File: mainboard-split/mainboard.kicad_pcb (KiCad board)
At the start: 2 copper layers, 171.7 x 109 mm, 24 parts, among them J1 3V3 IN, J2 Conn_01x04, J3 Conn_01x03, J4 Conn_01x02, J5 3V3 OUT, J6 STICK POWER, SW1 SW_SPDT_MSM, SW2 SW_SPDT_MSM, SW3 SW_Push, SW4 SW_Push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

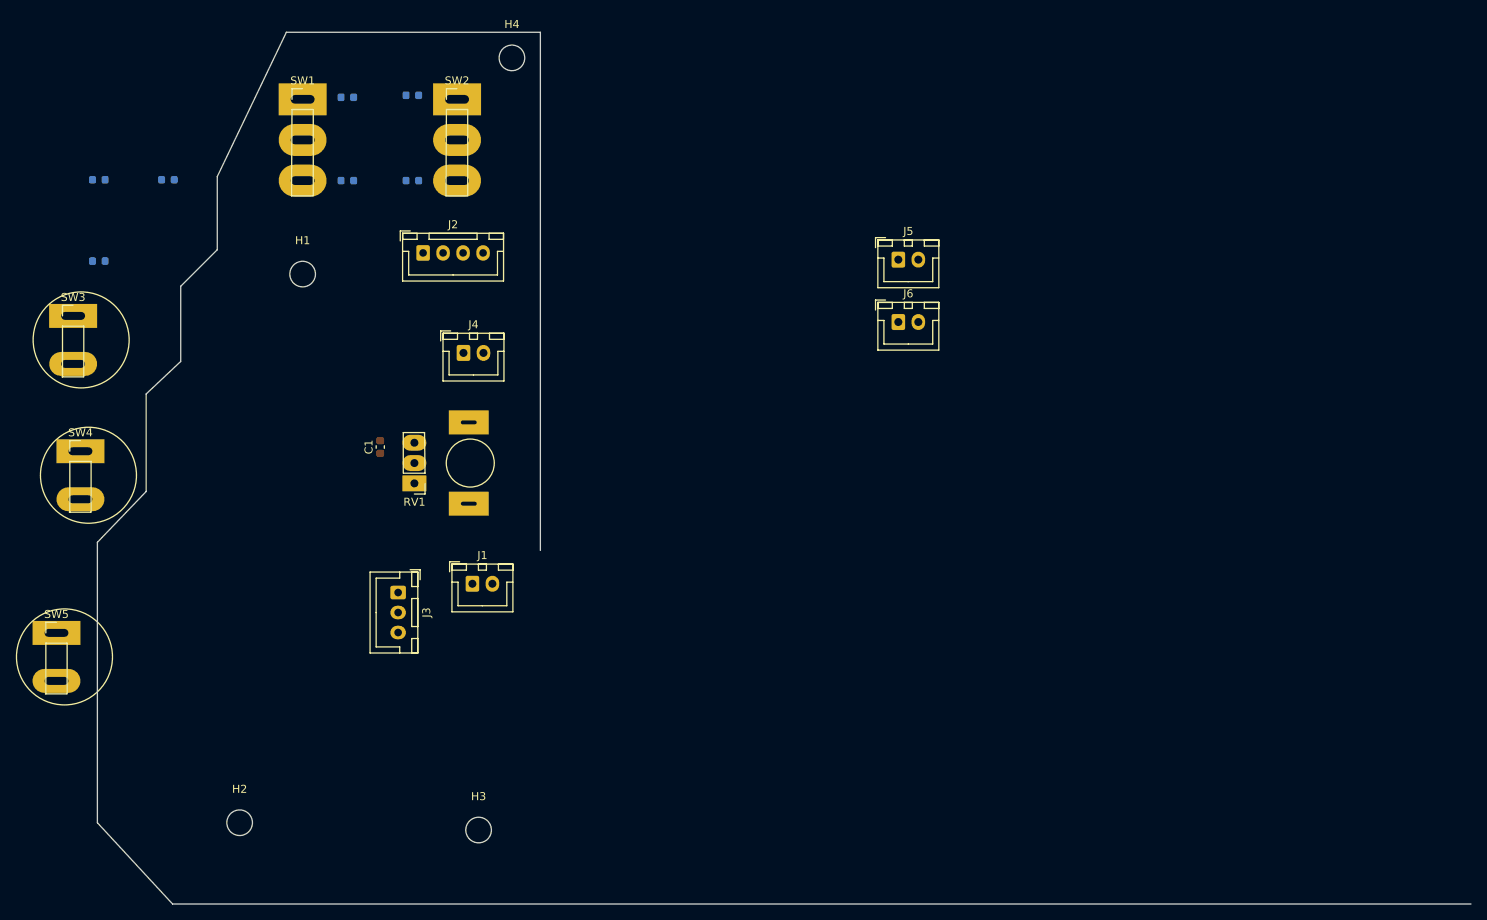
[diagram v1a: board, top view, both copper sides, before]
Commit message: Place switches on millimeter grid.
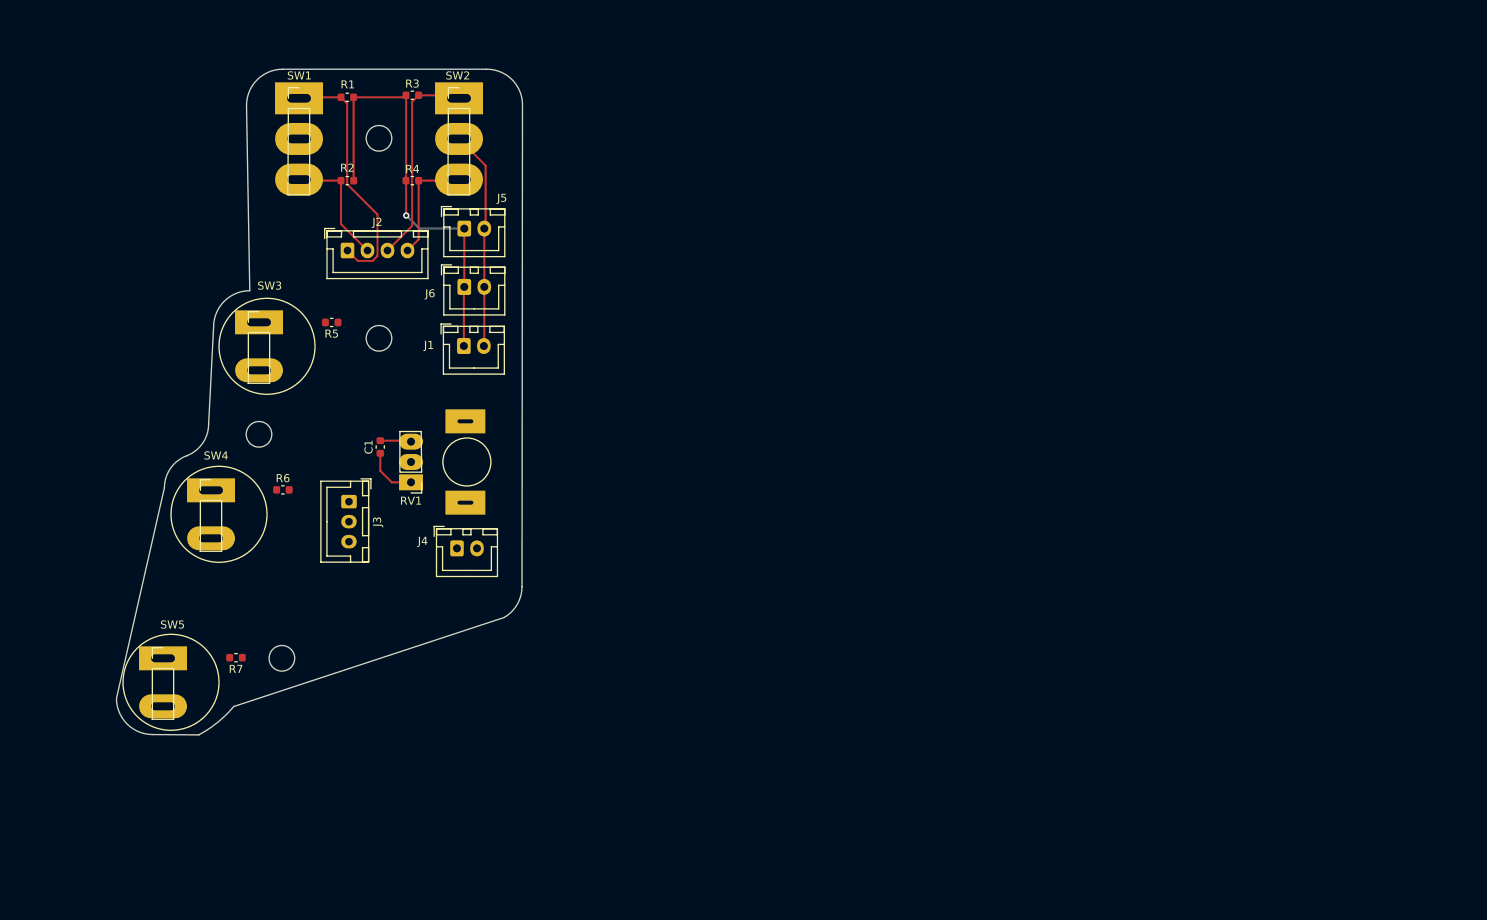
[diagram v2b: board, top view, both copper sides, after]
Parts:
- R1, R2, R3, R4, R5, R6, R7: moved to F.Cu
- moved R7 60.3 mm to (52.1, 204.9), turned to 180 degrees
- moved H3 56.6 mm to (55.0, 177.0)
- moved J6 54.4 mm to (80.7, 158.6)
- moved J5 54.4 mm to (80.7, 151.3)
- moved R6 36.7 mm to (58.0, 183.9), turned to 0 degrees
- moved R5 34.1 mm to (64.1, 163.0)
- moved J1 29.7 mm to (80.6, 166.0)
- moved J4 24.4 mm to (79.7, 191.3)
- moved SW3 23.2 mm to (55.0, 163.0)
- moved H2 21.2 mm to (57.9, 205.0)
- moved H4 19.4 mm to (70.0, 140.0)
- moved SW4 17.0 mm to (49.0, 184.0)
- moved SW5 13.7 mm to (43.0, 205.0)
- moved J3 12.9 mm to (66.2, 185.4)
- moved H1 12.5 mm to (70.0, 165.0)
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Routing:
- net +3V3: track 0.00 -> 61.4 mm, vias 0 -> 1
- net Net-(J2-Pin_1): track 0.00 -> 31.6 mm
- net GND: track 0.00 -> 31.2 mm
- net Net-(J2-Pin_3): track 0.00 -> 26.2 mm
- net Net-(J2-Pin_2): track 0.00 -> 15.4 mm
- net Net-(J2-Pin_4): track 0.00 -> 14.4 mm
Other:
- board size 171.7 x 109 mm -> 50.8 x 83.2 mm

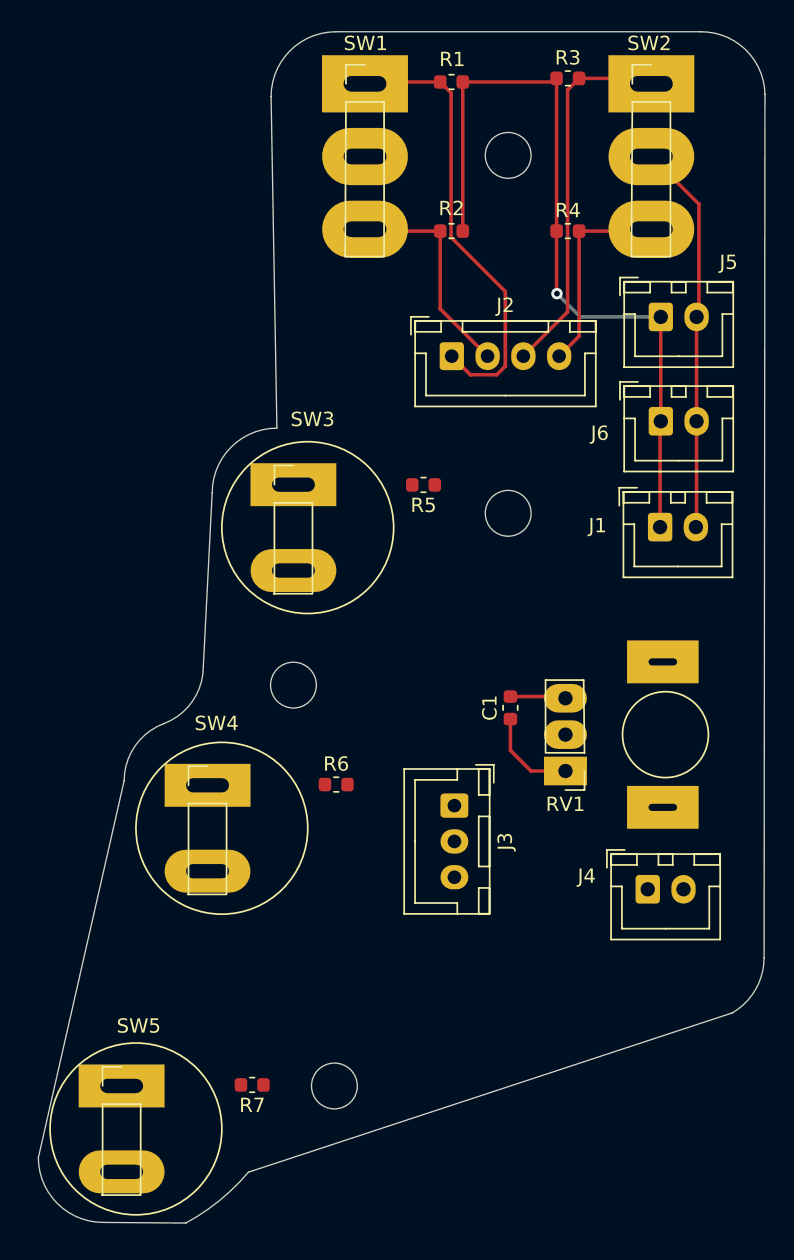
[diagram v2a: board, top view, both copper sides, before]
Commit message: Improve outline.
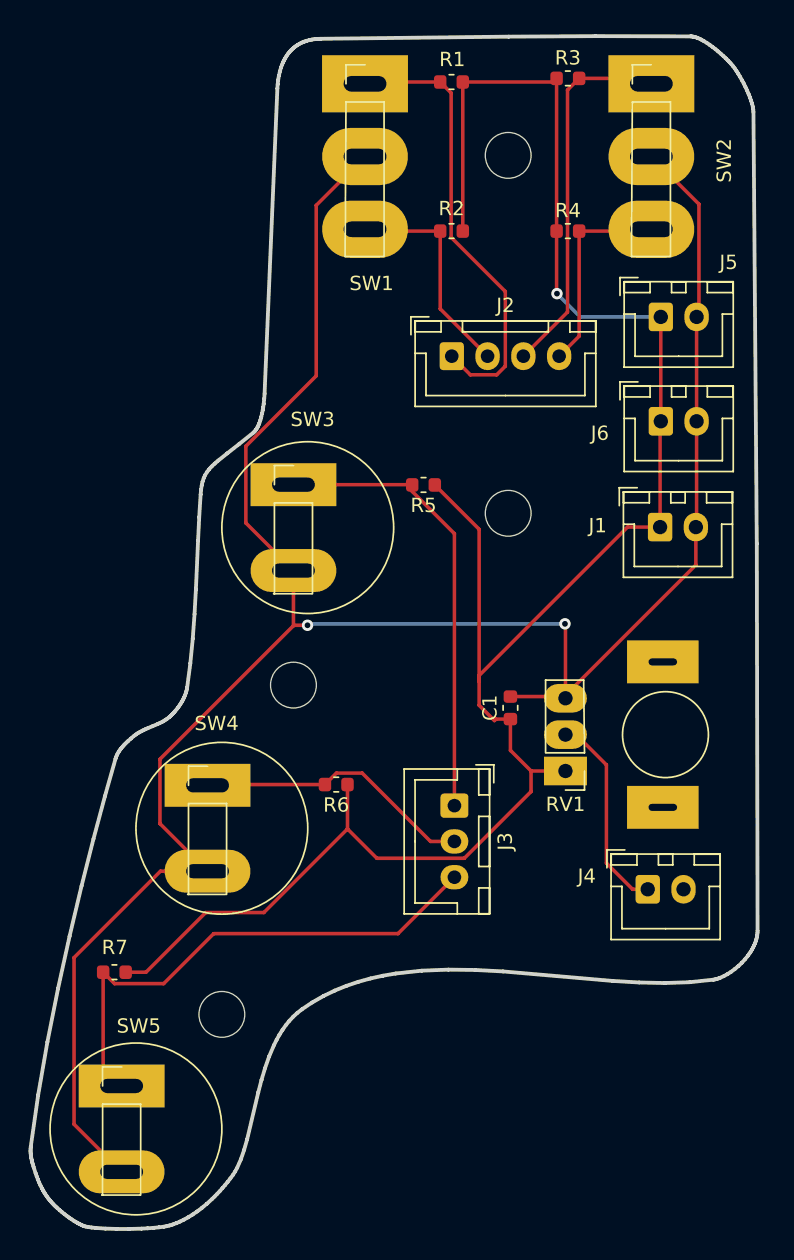
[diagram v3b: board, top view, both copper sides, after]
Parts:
- moved R7 12.4 mm to (42.5, 197.1)
- moved H2 9.32 mm to (50.0, 200.0)
- turned R6 to 180 degrees
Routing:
- net GND: track 31.2 -> 159.4 mm, vias 0 -> 2
- net +3V3: track 61.4 -> 137.8 mm
- net Net-(J3-Pin_3): track 0.00 -> 36.4 mm
- net Net-(J3-Pin_1): track 0.00 -> 31.9 mm
- net Net-(J3-Pin_2): track 0.00 -> 19.6 mm
- net A7: track 0.00 -> 14.2 mm
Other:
- board size 50.8 x 83.2 mm -> 50.8 x 83.3 mm

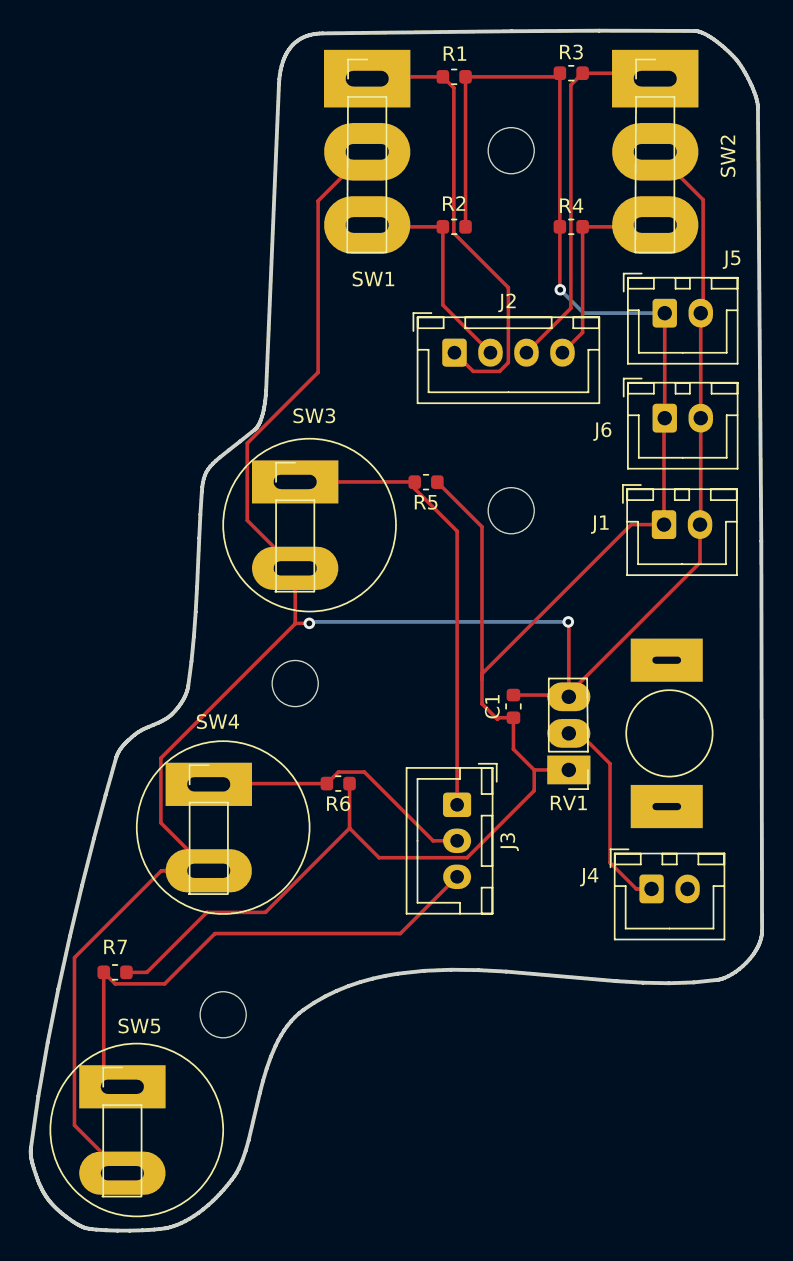
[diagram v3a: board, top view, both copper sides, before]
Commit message: Fix JST 3D models.
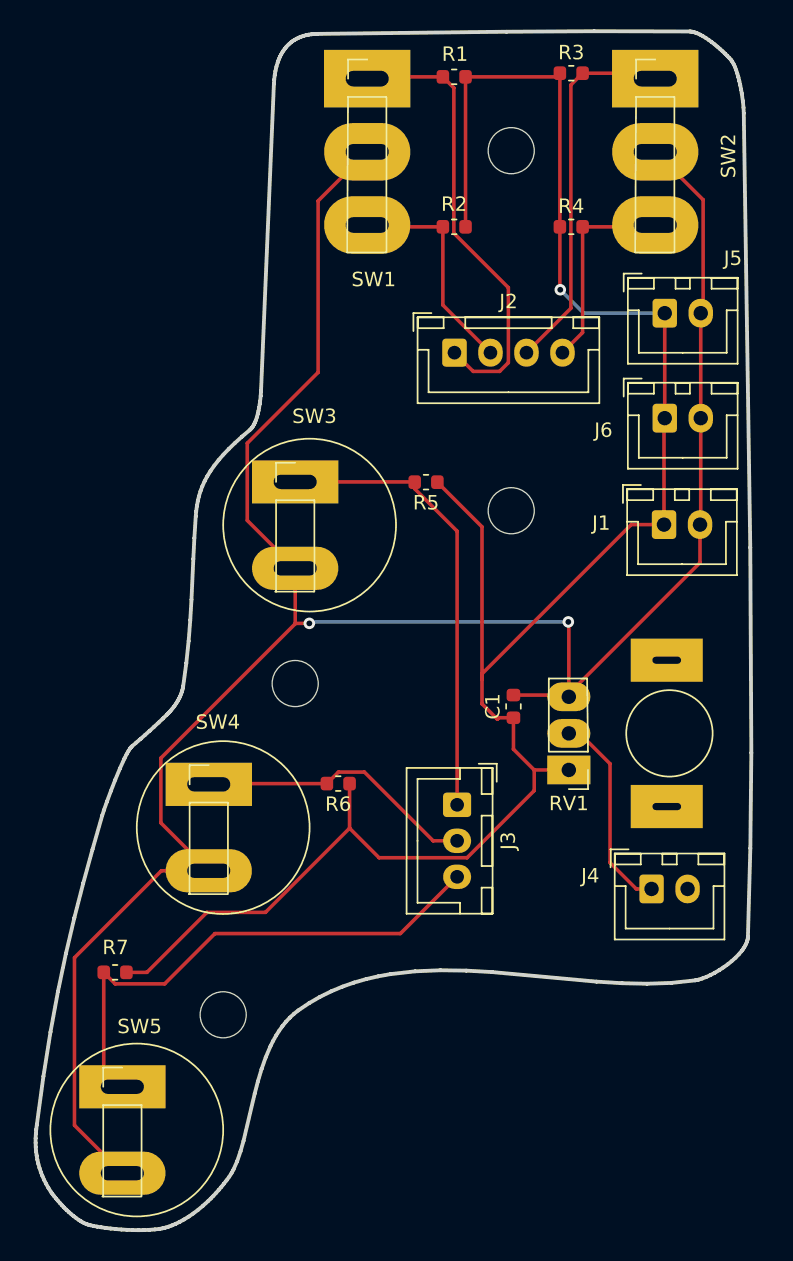
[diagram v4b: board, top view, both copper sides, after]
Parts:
- J1, J4, J5, J6: footprint Connector_JST:JST_XH_B02B-XH-A_1x02_P2.50mm_Vertical -> Connector_JST:JST_XH_B2B-XH-A_1x02_P2.50mm_Vertical
- J2: footprint Connector_JST:JST_XH_B04B-XH-A_1x04_P2.50mm_Vertical -> Connector_JST:JST_XH_B4B-XH-A_1x04_P2.50mm_Vertical
- J3: footprint Connector_JST:JST_XH_B03B-XH-A_1x03_P2.50mm_Vertical -> Connector_JST:JST_XH_B3B-XH-A_1x03_P2.50mm_Vertical
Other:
- board size 50.8 x 83.3 mm -> 49.7 x 83.3 mm
